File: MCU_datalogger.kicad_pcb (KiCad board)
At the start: 2 copper layers, 58.4 x 38.1 mm, 29 parts, among them J1 Conn_01x04_Pin, J2 Conn_01x09_Pin, J3 Conn_01x04_Pin, J4 Conn_02x03_Odd_Even, U1 24LC1025, U2 DS1337S_, U3 24LC1025, U4 ATMEGA328P-AU, Y1 32.768 KHz, Y2 16 MHz

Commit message: finished routing 4 layer pcb
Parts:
- turned Y2 to 0 degrees
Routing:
- net /SCK: track 0.00 -> 94.3 mm, vias 0 -> 5
- net /SDA: track 0.00 -> 57.7 mm, vias 0 -> 5
- net VCC: track 0.00 -> 45.6 mm, vias 0 -> 13
- net GND: track 0.00 -> 44.7 mm, vias 0 -> 11
- net /TX: track 0.00 -> 36.3 mm
- net /D2: track 0.00 -> 33.3 mm
- net /RX: track 0.00 -> 32.6 mm
- net /MOSI: track 0.00 -> 31.4 mm, vias 0 -> 2
- net Net-(U4-PB6): track 0.00 -> 29.2 mm, vias 0 -> 3
- net /D3: track 0.00 -> 29.1 mm
- net Net-(U4-PB7): track 0.00 -> 26.1 mm, vias 0 -> 3
- net /D4: track 0.00 -> 25.9 mm
- net /MISO: track 0.00 -> 25.0 mm, vias 0 -> 1
- net /D8: track 0.00 -> 24.7 mm
- net /RST_N: track 0.00 -> 24.6 mm, vias 0 -> 2
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- added copper zone on B.Cu, net GND
- added copper zone on In2.Cu, net VCC
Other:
- copper layers 2 -> 4

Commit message: finished silkscreen
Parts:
- added REF**: KiCad-Logo2_5mm_SilkScreen, Symbol:KiCad-Logo2_5mm_SilkScreen, B.Cu at (88.3, 97.1)
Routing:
- net /SCK: track 94.3 -> 94.9 mm
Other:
- board text added: "1"
- board text added: "2"
- board text added: "3"
- board text added: "4"
- board text added: "5"
- board text added: "6"
- board text added: "7"
- board text added: "GND"
- board text added: "GPIO"
- board text added: "I2C"
- board text added: "ICSP"
- board text added: "ISCP MISO|VCC SCK |MOSI RST |GND"
- board text added: "RX"
- board text added: "SCK"
- board text added: "SDA"
- board text added: "TX"
- board text added: "UART"
- board text added: "VCC"
- board text added: "by C.W. Wolfe"

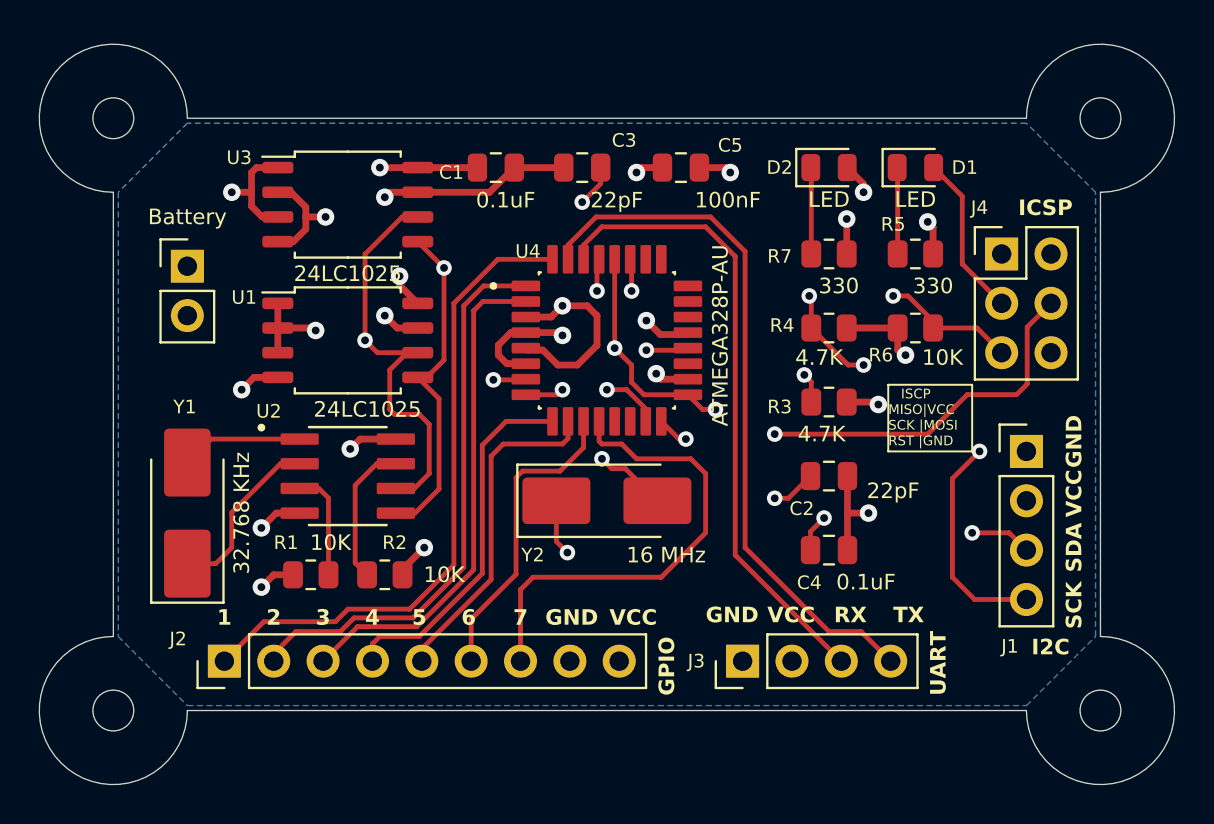
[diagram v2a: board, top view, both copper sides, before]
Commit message: fixed scl/sck issue in layout
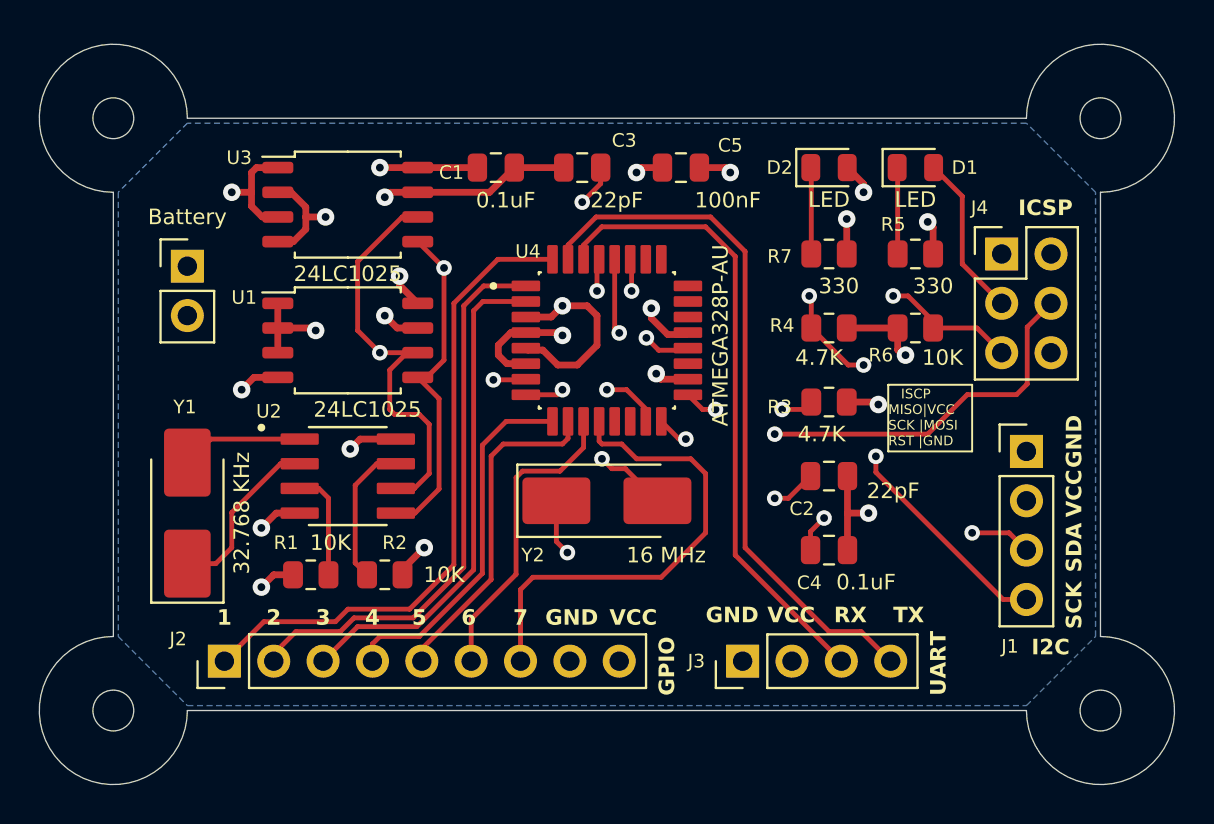
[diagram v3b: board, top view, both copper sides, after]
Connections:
- net Net-(U4-AREF) renamed /AREF
- J1 pad 4: /SCK -> /SCL
- R3 pad 2: /SCK -> /SCL
- U1 pad 6: /SCK -> /SCL
- U2 pad 6: /SCK -> /SCL
- U3 pad 6: /SCK -> /SCL
- U4 pad 28: /SCK -> /SCL
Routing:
- net /SCL: track 0.00 -> 67.8 mm, vias 0 -> 4
- net /SCK: track 94.9 -> 27.2 mm, vias 5 -> 1
- net /MISO: track 25.0 -> 23.8 mm
- net /AREF: track 21.3 -> 21.8 mm
